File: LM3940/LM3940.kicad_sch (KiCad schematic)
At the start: 9 parts, among them U1 LM317L_SOT-89

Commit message: Aggiunto R
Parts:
- added R? (x2): R, symbol pspice:R
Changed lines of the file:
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@@
+    (pin "2")
+  )
+  (symbol (lib_id "pspice:R") (at 140.97 123.19 0) (unit 1)
+    (in_bom yes) (on_board yes) (fields_autoplaced)
+    (property "Reference" "R?" (id 0) (at 143.51 121.9199 0)
+      (effects (font (size 1.27 1.27)) (justify left))
+    )
+    (property "Value" "R" (id 1) (at 143.51 124.4599 0)
+      (effects (font (size 1.27 1.27)) (justify left))
+    )
+    (property "Footprint" "" (id 2) (at 140.97 123.19 0)
+      (effects (font (size 1.27 1.27)) hide)
+    )
+    (property "Datasheet" "~" (id 3) (at 140.97 123.19 0)
+      (effects (font (size 1.27 1.27)) hide)
+    )
+    (pin "1")
     (pin "2")
   )
@@
     )
     (property "Datasheet" "~" (id 3) (at 124.46 67.31 0)
+      (effects (font (size 1.27 1.27)) hide)
+    )
+    (pin "1")
+    (pin "2")
+  )
+  (symbol (lib_id "pspice:R") (at 172.72 121.92 0) (unit 1)
+    (in_bom yes) (on_board yes) (fields_autoplaced)
+    (property "Reference" "R?" (id 0) (at 175.26 120.6499 0)
+      (effects (font (size 1.27 1.27)) (justify left))
+    )
+    (property "Value" "R" (id 1) (at 175.26 123.1899 0)
+      (effects (font (size 1.27 1.27)) (justify left))
+    )
+    (property "Footprint" "" (id 2) (at 172.72 121.92 0)
+      (effects (font (size 1.27 1.27)) hide)
+    )
+    (property "Datasheet" "~" (id 3) (at 172.72 121.92 0)
       (effects (font (size 1.27 1.27)) hide)
     )
@@
       (reference "R1") (unit 1) (value "240ohm") (footprint "")
     )
+    (path "/627a5da5-946e-4a29-a36a-24c5fe5443ba"
+      (reference "R?") (unit 1) (value "R") (footprint "")
+    )
+    (path "/e02eb89d-707b-4c8f-a075-b16cf874877b"
+      (reference "R?") (unit 1) (value "R") (footprint "")
+    )
     (path "/403eef28-9046-4fbe-866a-40b766deda5f"

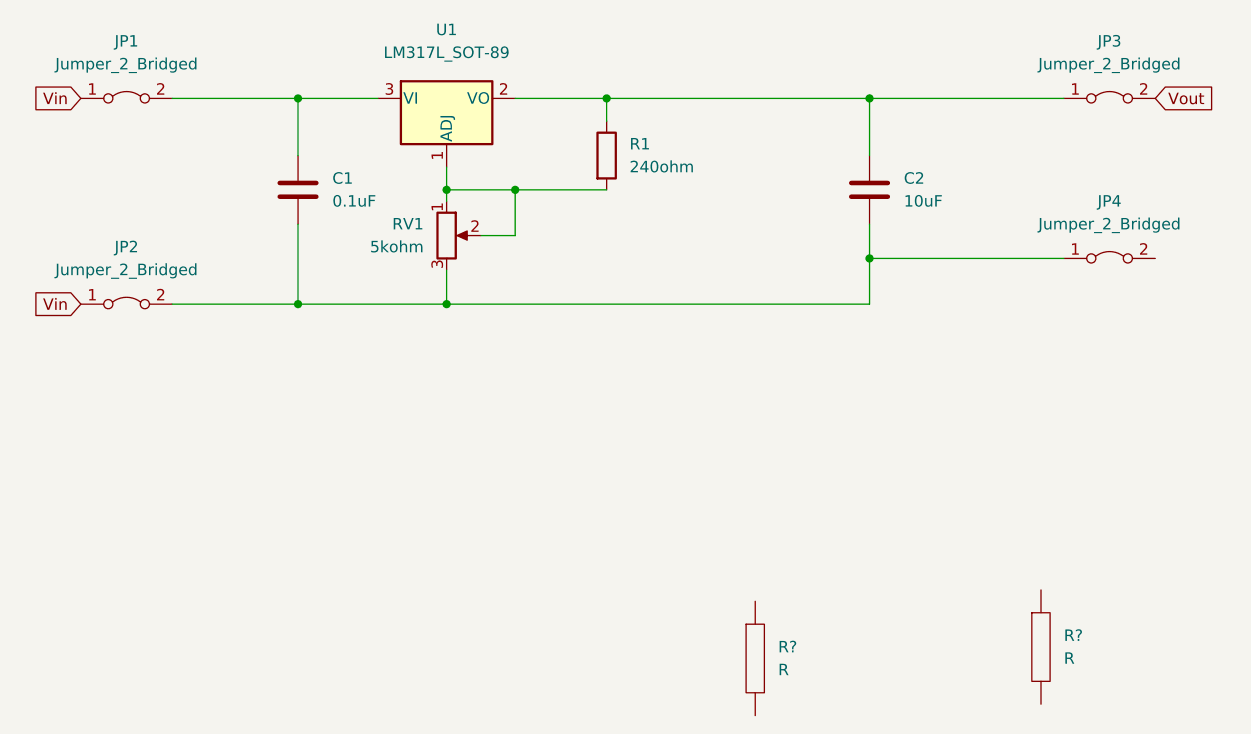
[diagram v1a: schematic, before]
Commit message: Cancellato le resistenze
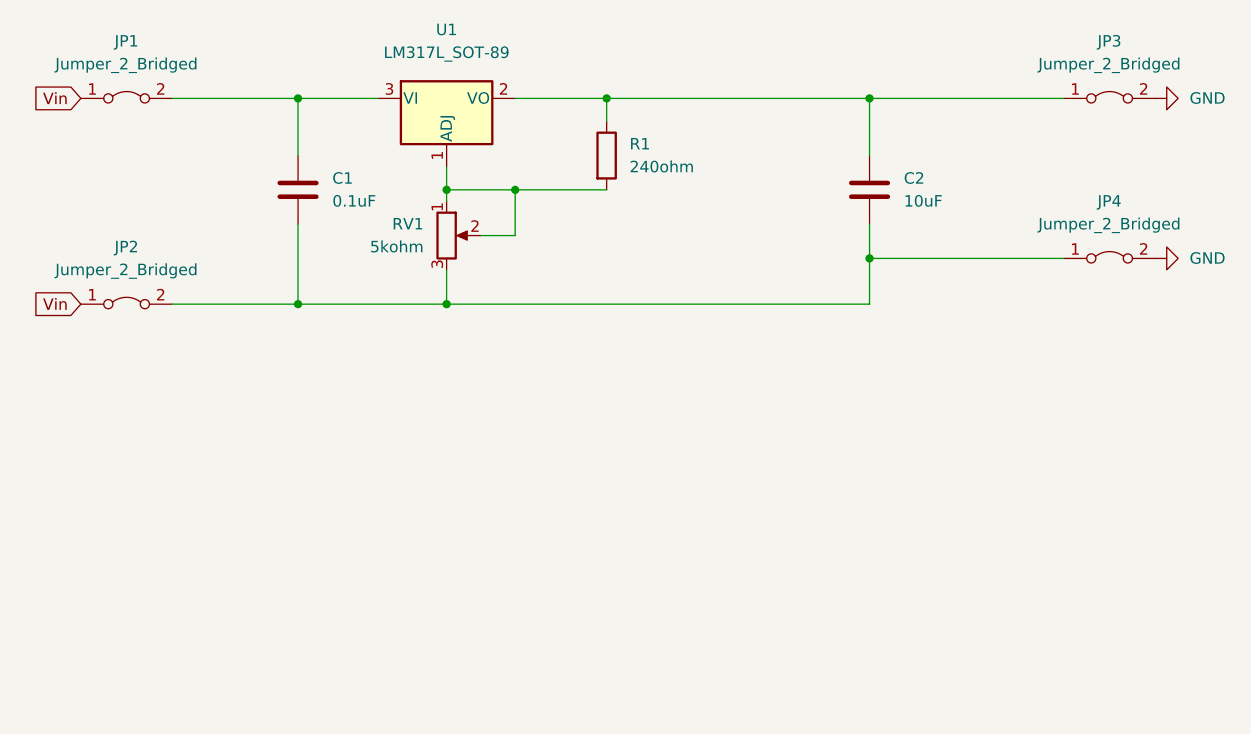
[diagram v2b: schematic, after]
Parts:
- removed R? (x2): R, symbol pspice:R
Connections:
- net Vout is gone; now on net GND: JP3.2 (B)
- net GND: now reaches JP4.2 (B)
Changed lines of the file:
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@@
     (stroke (width 0) (type default) (color 0 0 0 0))
-  )
-  (global_label "Vout" (shape input) (at 185.42 60.96 0) (fields_autoplaced)
-    (effects (font (size 1.27 1.27)) (justify left))
-    (property "Intersheet References" "${INTERSHEET_REFS}" (id 0) (at 191.9455 60.8806 0)
-      (effects (font (size 1.27 1.27)) (justify left) hide)
-    )
   )
   (global_label "Vin" (shape input) (at 66.04 60.96 180) (fields_autoplaced)
@@
     (pin "2")
   )
+  (symbol (lib_id "power:GND") (at 185.42 78.74 90) (unit 1)
+    (in_bom yes) (on_board yes) (fields_autoplaced)
+    (property "Reference" "#PWR?" (id 0) (at 191.77 78.74 0)
+      (effects (font (size 1.27 1.27)) hide)
+    )
+    (property "Value" "GND" (id 1) (at 189.23 78.7399 90)
+      (effects (font (size 1.27 1.27)) (justify right))
+    )
+    (property "Footprint" "" (id 2) (at 185.42 78.74 0)
+      (effects (font (size 1.27 1.27)) hide)
+    )
+    (property "Datasheet" "" (id 3) (at 185.42 78.74 0)
+      (effects (font (size 1.27 1.27)) hide)
+    )
+    (pin "1")
+  )
   (symbol (lib_id "Device:C") (at 90.17 71.12 0) (unit 1)
     (in_bom yes) (on_board yes) (fields_autoplaced)
@@
     (pin "2")
   )
-  (symbol (lib_id "pspice:R") (at 140.97 123.19 0) (unit 1)
-    (in_bom yes) (on_board yes) (fields_autoplaced)
-    (property "Reference" "R?" (id 0) (at 143.51 121.9199 0)
-      (effects (font (size 1.27 1.27)) (justify left))
-    )
-    (property "Value" "R" (id 1) (at 143.51 124.4599 0)
-      (effects (font (size 1.27 1.27)) (justify left))
-    )
-    (property "Footprint" "" (id 2) (at 140.97 123.19 0)
-      (effects (font (size 1.27 1.27)) hide)
-    )
-    (property "Datasheet" "~" (id 3) (at 140.97 123.19 0)
-      (effects (font (size 1.27 1.27)) hide)
-    )
-    (pin "1")
-    (pin "2")
+  (symbol (lib_id "power:GND") (at 185.42 60.96 90) (unit 1)
+    (in_bom yes) (on_board yes) (fields_autoplaced)
+    (property "Reference" "#PWR?" (id 0) (at 191.77 60.96 0)
+      (effects (font (size 1.27 1.27)) hide)
+    )
+    (property "Value" "GND" (id 1) (at 189.23 60.9599 90)
+      (effects (font (size 1.27 1.27)) (justify right))
+    )
+    (property "Footprint" "" (id 2) (at 185.42 60.96 0)
+      (effects (font (size 1.27 1.27)) hide)
+    )
+    (property "Datasheet" "" (id 3) (at 185.42 60.96 0)
+      (effects (font (size 1.27 1.27)) hide)
+    )
+    (pin "1")
   )
   (symbol (lib_id "Jumper:Jumper_2_Bridged") (at 180.34 60.96 0) (unit 1)
@@
     )
     (property "Datasheet" "~" (id 3) (at 124.46 67.31 0)
-      (effects (font (size 1.27 1.27)) hide)
-    )
-    (pin "1")
-    (pin "2")
-  )
-  (symbol (lib_id "pspice:R") (at 172.72 121.92 0) (unit 1)
-    (in_bom yes) (on_board yes) (fields_autoplaced)
-    (property "Reference" "R?" (id 0) (at 175.26 120.6499 0)
-      (effects (font (size 1.27 1.27)) (justify left))
-    )
-    (property "Value" "R" (id 1) (at 175.26 123.1899 0)
-      (effects (font (size 1.27 1.27)) (justify left))
-    )
-    (property "Footprint" "" (id 2) (at 172.72 121.92 0)
-      (effects (font (size 1.27 1.27)) hide)
-    )
-    (property "Datasheet" "~" (id 3) (at 172.72 121.92 0)
       (effects (font (size 1.27 1.27)) hide)
     )
@@
   )
   (symbol_instances
+    (path "/12b92dab-e465-4b58-8170-59107de8b61a"
+      (reference "#PWR?") (unit 1) (value "GND") (footprint "")
+    )
+    (path "/625099ef-f050-42f6-ae1b-f5242f2663af"
+      (reference "#PWR?") (unit 1) (value "GND") (footprint "")
+    )
     (path "/16827c54-c9b4-4ced-9372-0aa6bd8a5213"
       (reference "C1") (unit 1) (value "0.1uF") (footprint "")
@@
       (reference "R1") (unit 1) (value "240ohm") (footprint "")
     )
-    (path "/627a5da5-946e-4a29-a36a-24c5fe5443ba"
-      (reference "R?") (unit 1) (value "R") (footprint "")
-    )
-    (path "/e02eb89d-707b-4c8f-a075-b16cf874877b"
-      (reference "R?") (unit 1) (value "R") (footprint "")
-    )
     (path "/403eef28-9046-4fbe-866a-40b766deda5f"
